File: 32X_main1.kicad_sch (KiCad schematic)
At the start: 26 parts, among them IC504 315-5818, IC505 315-5805, IC509 74AC04

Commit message: General tidying.
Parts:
- removed C912: 10uF, Capacitor_THT:CP_Radial_D5.0mm_P2.50mm, symbol Device:C_Polarized
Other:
- moved on the sheet: C912
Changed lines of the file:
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@@
   (junction (at 96.52 65.405) (diameter 0) (color 0 0 0 0)
   )
-  (junction (at 231.14 250.19) (diameter 0) (color 0 0 0 0)
-  )
   (junction (at 266.7 169.545) (diameter 0) (color 0 0 0 0)
   )
@@
   )
   (junction (at 96.52 79.375) (diameter 0) (color 0 0 0 0)
-  )
-  (junction (at 231.14 238.125) (diameter 0) (color 0 0 0 0)
   )
   (junction (at 96.52 106.68) (diameter 0) (color 0 0 0 0)
@@
     (stroke (width 0) (type default))
   )
-  (wire (pts (xy 231.14 250.19) (xy 243.205 250.19))
-    (stroke (width 0) (type default))
-  )
   (bus (pts (xy 222.885 151.765) (xy 222.885 154.305))
     (stroke (width 0) (type default))
@@
     (stroke (width 0) (type default))
   )
-  (wire (pts (xy 231.14 238.125) (xy 231.14 240.03))
-    (stroke (width 0) (type default))
-  )
   (bus (pts (xy 203.2 83.185) (xy 203.2 80.645))
     (stroke (width 0) (type default))
@@
     (stroke (width 0) (type default))
   )
-  (wire (pts (xy 220.345 250.19) (xy 231.14 250.19))
+  (wire (pts (xy 220.345 250.19) (xy 232.41 250.19))
     (stroke (width 0) (type default))
   )
@@
     (stroke (width 0) (type default))
   )
-  (wire (pts (xy 243.205 238.125) (xy 243.205 240.03))
+  (wire (pts (xy 232.41 238.125) (xy 232.41 240.03))
     (stroke (width 0) (type default))
   )
@@
     (stroke (width 0) (type default))
   )
-  (wire (pts (xy 231.14 250.19) (xy 231.14 247.65))
-    (stroke (width 0) (type default))
-  )
   (wire (pts (xy 90.805 84.455) (xy 96.52 84.455))
     (stroke (width 0) (type default))
@@
     (stroke (width 0) (type default))
   )
-  (wire (pts (xy 243.205 250.19) (xy 243.205 247.65))
+  (wire (pts (xy 232.41 250.19) (xy 232.41 247.65))
     (stroke (width 0) (type default))
   )
@@
     (stroke (width 0) (type default))
   )
-  (wire (pts (xy 220.345 238.125) (xy 231.14 238.125))
-    (stroke (width 0) (type default))
-  )
   (bus (pts (xy 222.885 146.685) (xy 222.885 149.225))
     (stroke (width 0) (type default))
@@
     (stroke (width 0) (type default))
   )
-  (wire (pts (xy 231.14 238.125) (xy 243.205 238.125))
+  (wire (pts (xy 220.345 238.125) (xy 232.41 238.125))
     (stroke (width 0) (type default))
   )
@@
     )
   )
-  (symbol (lib_id "Device:C_Polarized") (at 231.14 243.84 0) (unit 1)
-    (in_bom yes) (on_board yes) (dnp no)
-    (property "Reference" "C912" (at 234.315 245.11 0)
-      (effects (font (size 1.27 1.27)) (justify left))
-    )
-    (property "Value" "10uF" (at 234.315 242.57 0)
-      (effects (font (size 1.27 1.27)) (justify left))
-    )
-    (property "Footprint" "Capacitor_THT:CP_Radial_D5.0mm_P2.50mm" (at 232.1052 247.65 0)
-      (effects (font (size 1.27 1.27)) hide)
-    )
-    (property "Datasheet" "~" (at 231.14 243.84 0)
-      (effects (font (size 1.27 1.27)) hide)
-    )
-    (property "DigiKey" "" (at 231.14 243.84 0)
-      (effects (font (size 1.27 1.27)) hide)
-    )
-    (pin "1")
-    (pin "2")
-    (instances
-      (project "Neptune"
-        (path "/bcc23b51-b742-4ae5-9dd6-d96a24058944/01513199-62c5-4123-a151-ccd381a5e6c1"
-          (reference "C912") (unit 1)
-        )
-        (path "/bcc23b51-b742-4ae5-9dd6-d96a24058944/293c8f1f-2c58-4557-aeb8-8502bb66fbd4"
-          (reference "CE21") (unit 1)
-        )
-        (path "/bcc23b51-b742-4ae5-9dd6-d96a24058944/48e60f61-77cc-4ea0-898f-0029aa970ca5"
-          (reference "CE20") (unit 1)
-        )
-        (path "/bcc23b51-b742-4ae5-9dd6-d96a24058944/0d895458-d3d0-4635-bde5-e15500822f5f"
-          (reference "C30") (unit 1)
-        )
-        (path "/bcc23b51-b742-4ae5-9dd6-d96a24058944/a9caee2e-423b-443e-a11f-5841882e2685"
-          (reference "CE501") (unit 1)
-        )
-      )
-    )
-  )
   (symbol (lib_id "Device:C") (at 195.58 243.84 0) (unit 1)
     (in_bom yes) (on_board yes) (dnp no)
@@
     )
   )
-  (symbol (lib_id "Device:C_Polarized") (at 243.205 243.84 0) (unit 1)
+  (symbol (lib_id "Device:C_Polarized") (at 232.41 243.84 0) (unit 1)
     (in_bom yes) (on_board yes) (dnp no)
-    (property "Reference" "C912" (at 246.38 245.11 0)
+    (property "Reference" "C912" (at 235.585 245.11 0)
       (effects (font (size 1.27 1.27)) (justify left))
     )
-    (property "Value" "10uF" (at 246.38 242.57 0)
+    (property "Value" "10uF" (at 235.585 242.57 0)
       (effects (font (size 1.27 1.27)) (justify left))
     )
-    (property "Footprint" "Capacitor_THT:CP_Radial_D5.0mm_P2.50mm" (at 244.1702 247.65 0)
-      (effects (font (size 1.27 1.27)) hide)
-    )
-    (property "Datasheet" "~" (at 243.205 243.84 0)
-      (effects (font (size 1.27 1.27)) hide)
-    )
-    (property "DigiKey" "" (at 243.205 243.84 0)
-      (effects (font (size 1.27 1.27)) hide)
-    )
+    (property "Footprint" "Capacitor_THT:CP_Radial_D5.0mm_P2.50mm" (at 233.3752 247.65 0)
+      (effects (font (size 1.27 1.27)) hide)
+    )
+    (property "Datasheet" "~" (at 232.41 243.84 0)
+      (effects (font (size 1.27 1.27)) hide)
+    )
+    (property "DigiKey" "" (at 232.41 243.84 0)
+      (effects (font (size 1.27 1.27)) hide)
+    )

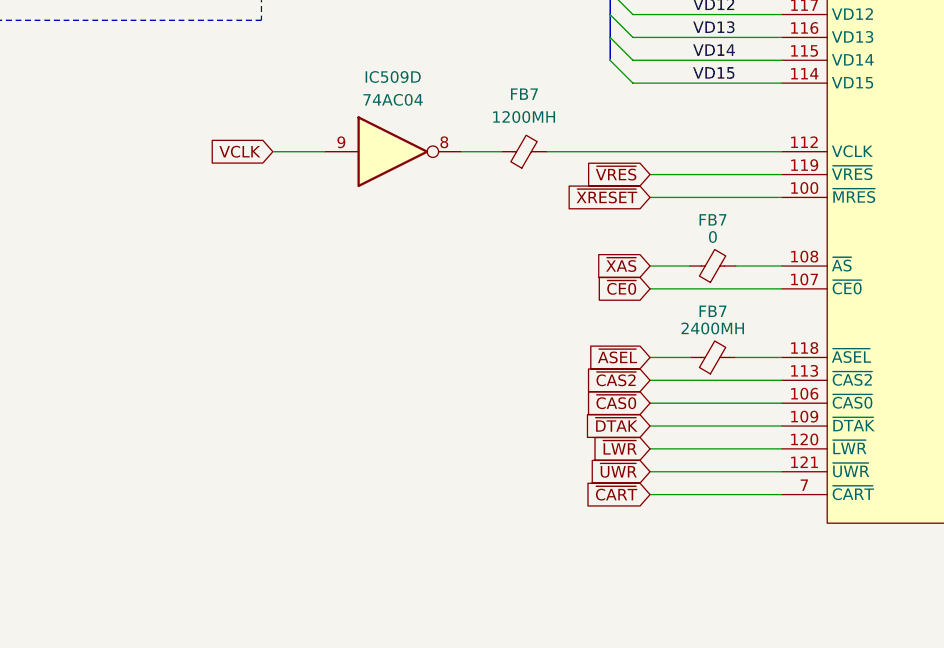
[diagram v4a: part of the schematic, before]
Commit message: Footprint improvements, general tidying.
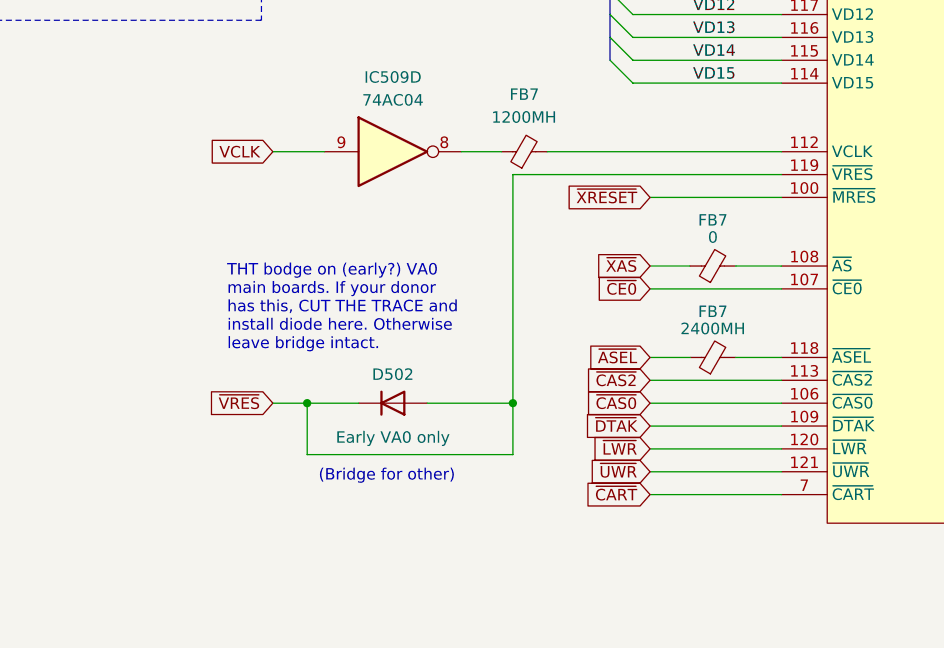
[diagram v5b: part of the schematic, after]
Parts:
- added D502: Early VA0 only, Diode_SMD:D_1206_3216Metric, symbol Device:D
- IC504: footprint Package_QFP:LQFP-176_24x24mm_P0.5mm -> Neptune:LQFP-176_24x24mm_P0.5mm
- L501: footprint Inductor_SMD:L_1206_3216Metric -> Inductor_SMD:L_1210_3225Metric_Pad1.42x2.65mm_HandSolder
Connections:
- net ~{VRES}: now also D502.1 (K), D502.2 (A)
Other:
- note added: "(Bridge for other)"
- note added: "THT bodge on (early?) VA0 main boards. If your donor has this, CUT THE TRACE and install diode here. Otherwise leave bridge intact."
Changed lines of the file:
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@@
   (junction (at 266.7 169.545) (diameter 0) (color 0 0 0 0)
   )
+  (junction (at 131.445 184.785) (diameter 0) (color 0 0 0 0)
+  )
   (junction (at 96.52 67.945) (diameter 0) (color 0 0 0 0)
   )
@@
   (junction (at 96.52 120.65) (diameter 0) (color 0 0 0 0)
   )
+  (junction (at 108.585 184.785) (diameter 0) (color 0 0 0 0)
+  )
   (junction (at 203.835 177.165) (diameter 0) (color 0 0 0 0)
   )
@@
     (stroke (width 0) (type default))
   )
+  (wire (pts (xy 104.775 184.785) (xy 108.585 184.785))
+    (stroke (width 0) (type default))
+  )
   (bus (pts (xy 203.2 67.945) (xy 203.2 65.405))
     (stroke (width 0) (type default))
@@
     (stroke (width 0) (type default))
   )
-  (wire (pts (xy 146.685 159.385) (xy 161.29 159.385))
-    (stroke (width 0) (type default))
-  )
   (wire (pts (xy 191.77 80.645) (xy 200.66 80.645))
     (stroke (width 0) (type default))
@@
     (stroke (width 0) (type default))
   )
+  (wire (pts (xy 121.92 184.785) (xy 131.445 184.785))
+    (stroke (width 0) (type default))
+  )
+  (wire (pts (xy 108.585 184.785) (xy 114.3 184.785))
+    (stroke (width 0) (type default))
+  )
   (bus (pts (xy 203.2 78.105) (xy 203.2 75.565))
     (stroke (width 0) (type default))
@@
     (stroke (width 0) (type default))
   )
+  (wire (pts (xy 131.445 159.385) (xy 131.445 184.785))
+    (stroke (width 0) (type default))
+  )
   (wire (pts (xy 194.945 177.165) (xy 203.835 177.165))
     (stroke (width 0) (type default))
@@
     (stroke (width 0) (type default))
   )
+  (wire (pts (xy 108.585 190.5) (xy 108.585 184.785))
+    (stroke (width 0) (type default))
+  )
   (wire (pts (xy 264.795 50.165) (xy 273.685 50.165))
     (stroke (width 0) (type default))
@@
     (stroke (width 0) (type default))
   )
+  (wire (pts (xy 131.445 159.385) (xy 161.29 159.385))
+    (stroke (width 0) (type default))
+  )
   (wire (pts (xy 234.315 159.385) (xy 225.425 159.385))
     (stroke (width 0) (type default))
@@
     (stroke (width 0) (type default))
   )
+  (wire (pts (xy 131.445 184.785) (xy 131.445 190.5))
+    (stroke (width 0) (type default))
+  )
   (wire (pts (xy 194.945 151.765) (xy 194.945 154.305))
     (stroke (width 0) (type default))
@@
     (stroke (width 0) (type default))
   )
+  (wire (pts (xy 131.445 190.5) (xy 108.585 190.5))
+    (stroke (width 0) (type default))
+  )
   (bus (pts (xy 203.2 47.625) (xy 203.2 50.165))
     (stroke (width 0) (type default))
@@
     (fill (type none))
   )
+  (text "(Bridge for other)" (at 109.855 193.675 0)
+    (effects (font (size 1.27 1.27)) (justify left bottom))
+  )
   (text "VA1 ONLY" (at 91.44 49.53 0)
     (effects (font (size 1.27 1.27)) (justify left bottom))
   )
+  (text "THT bodge on (early?) VA0\nmain boards. If your donor\nhas this, CUT THE TRACE and\ninstall diode here. Otherwise\nleave bridge intact."
+    (at 99.695 179.07 0)
+    (effects (font (size 1.27 1.27)) (justify left bottom))
+  )
   (label "CTD6" (at 194.31 65.405 0) (fields_autoplaced)
     (effects (font (size 1.27 1.27)) (justify left bottom))
@@
     )
   )
-  (global_label "~{VRES}" (shape input) (at 146.685 159.385 180) (fields_autoplaced)
+  (global_label "~{VRES}" (shape input) (at 104.775 184.785 180) (fields_autoplaced)
     (effects (font (size 1.27 1.27)) (justify right))
-    (property "Intersheetrefs" "${INTERSHEET_REFS}" (at 138.9827 159.385 0)
+    (property "Intersheetrefs" "${INTERSHEET_REFS}" (at 97.0727 184.785 0)
       (effects (font (size 1.27 1.27)) (justify right) hide)
     )
@@
     )
   )
+  (symbol (lib_id "Device:D") (at 118.11 184.785 0) (mirror x) (unit 1)
+    (in_bom yes) (on_board yes) (dnp no)
+    (property "Reference" "D502" (at 118.11 181.61 0)
+      (effects (font (size 1.27 1.27)))
+    )
+    (property "Value" "Early VA0 only" (at 118.11 188.595 0)
+      (effects (font (size 1.27 1.27)))
+    )
+    (property "Footprint" "Diode_SMD:D_1206_3216Metric" (at 118.11 184.785 0)
+      (effects (font (size 1.27 1.27)) hide)
+    )
+    (property "Datasheet" "~" (at 118.11 184.785 0)
+      (effects (font (size 1.27 1.27)) hide)
+    )
+    (property "Sim.Device" "D" (at 118.11 184.785 0)
+      (effects (font (size 1.27 1.27)) hide)
+    )
+    (property "Sim.Pins" "1=K 2=A" (at 118.11 184.785 0)
+      (effects (font (size 1.27 1.27)) hide)
+    )
+    (property "DigiKey" "" (at 118.11 184.785 0)
+      (effects (font (size 1.27 1.27)) hide)
+    )
+    (pin "1")
+    (pin "2")
+    (instances
+      (project "Neptune"
+        (path "/bcc23b51-b742-4ae5-9dd6-d96a24058944/edde10e2-ce08-4180-9fbe-ab298dfbfa4c"
+          (reference "D502") (unit 1)
+        )
+        (path "/bcc23b51-b742-4ae5-9dd6-d96a24058944/01513199-62c5-4123-a151-ccd381a5e6c1"
+          (reference "D599") (unit 1)
+        )
+        (path "/bcc23b51-b742-4ae5-9dd6-d96a24058944/a9caee2e-423b-443e-a11f-5841882e2685"
+          (reference "D699") (unit 1)
+        )
+      )
+    )
+  )
   (symbol (lib_id "Device:C_Polarized") (at 232.41 243.84 0) (unit 1)
     (in_bom yes) (on_board yes) (dnp no)
@@
       (effects (font (size 1.27 1.27)) (justify left))
     )
-    (property "Footprint" "Inductor_SMD:L_1206_3216Metric" (at 203.835 170.815 0)
+    (property "Footprint" "Inductor_SMD:L_1210_3225Metric_Pad1.42x2.65mm_HandSolder" (at 203.835 170.815 0)
       (effects (font (size 1.27 1.27)) hide)
     )
@@
       (effects (font (size 1.27 1.27)))
     )
-    (property "Footprint" "Package_QFP:LQFP-176_24x24mm_P0.5mm" (at 176.53 48.26 0)
+    (property "Footprint" "Neptune:LQFP-176_24x24mm_P0.5mm" (at 176.53 48.26 0)
       (effects (font (size 1.27 1.27)) hide)
     )

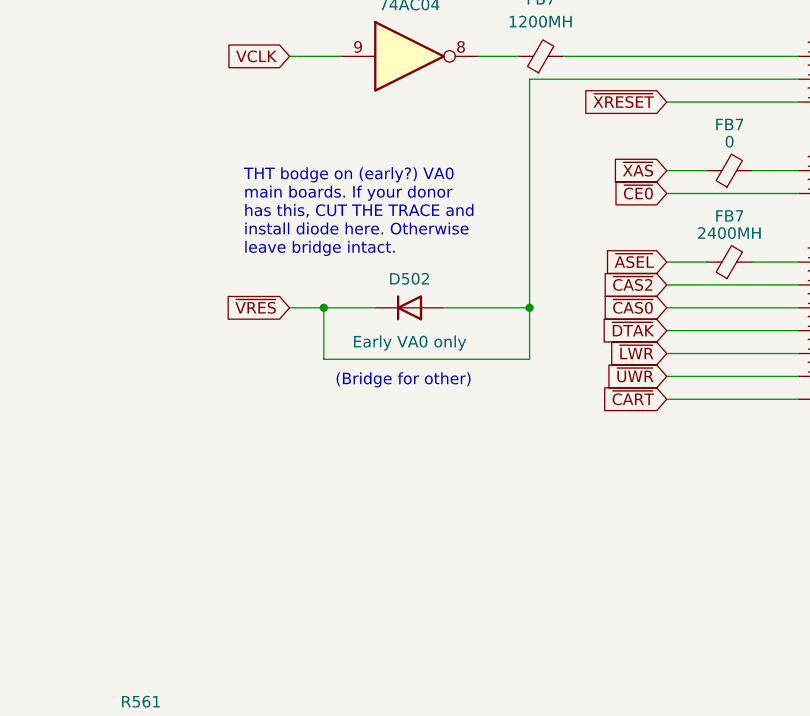
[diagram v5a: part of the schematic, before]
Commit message: Fix note about D699, add footprint for associated capacitor.
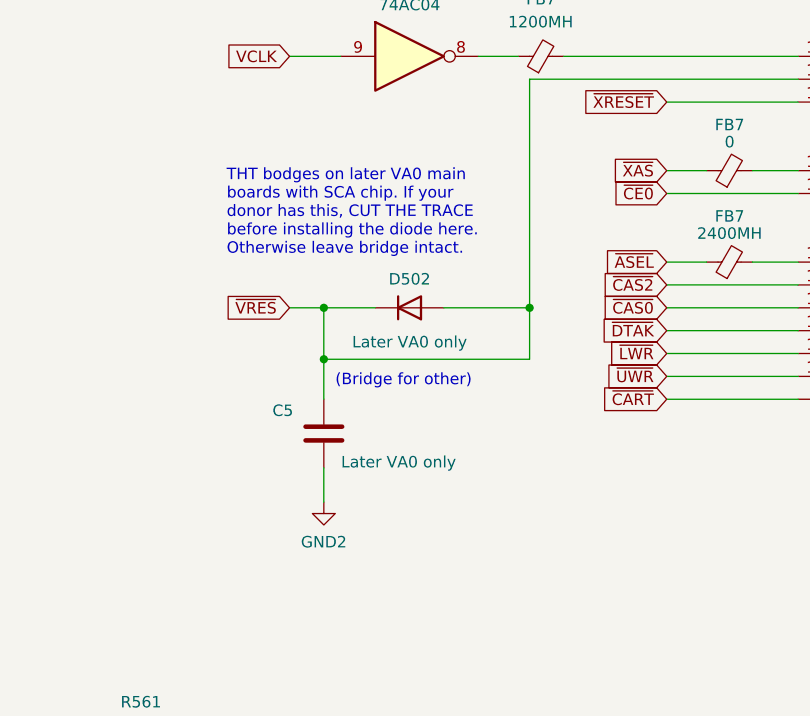
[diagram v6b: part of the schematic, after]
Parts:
- added C5: Later VA0 only, Capacitor_SMD:C_0805_2012Metric, symbol Device:C
- D502: value Early VA0 only -> Later VA0 only
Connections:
- net GND2: now also C5.2
- net ~{VRES}: now also C5.1
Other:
- note added: "THT bodges on later VA0 main boards with SCA chip. If your donor has this, CUT THE TRACE before installing the diode here. Otherwise leave bridge intact."
- note removed: "THT bodge on (early?) VA0 main boards. If your donor has this, CUT THE TRACE and install diode here. Otherwise leave bridge intact."
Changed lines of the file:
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@@
   (junction (at 282.575 151.765) (diameter 0) (color 0 0 0 0)
   )
+  (junction (at 108.585 190.5) (diameter 0) (color 0 0 0 0)
+  )
   (junction (at 266.7 172.085) (diameter 0) (color 0 0 0 0)
   )
@@
     (stroke (width 0) (type default))
   )
+  (wire (pts (xy 108.585 202.565) (xy 108.585 206.375))
+    (stroke (width 0) (type default))
+  )
   (wire (pts (xy 234.315 90.805) (xy 225.425 90.805))
     (stroke (width 0) (type default))
@@
     (stroke (width 0) (type default))
   )
+  (wire (pts (xy 108.585 190.5) (xy 108.585 194.945))
+    (stroke (width 0) (type default))
+  )
   (wire (pts (xy 207.645 238.125) (xy 220.345 238.125))
     (stroke (width 0) (type default))
@@
     (effects (font (size 1.27 1.27)) (justify left bottom))
   )
-  (text "THT bodge on (early?) VA0\nmain boards. If your donor\nhas this, CUT THE TRACE and\ninstall diode here. Otherwise\nleave bridge intact."
-    (at 99.695 179.07 0)
+  (text "THT bodges on later VA0 main\nboards with SCA chip. If your\ndonor has this, CUT THE TRACE\nbefore installing the diode here.\nOtherwise leave bridge intact."
+    (at 97.79 179.07 0)
     (effects (font (size 1.27 1.27)) (justify left bottom))
   )
@@
     )
   )
+  (symbol (lib_id "Device:C") (at 108.585 198.755 0) (unit 1)
+    (in_bom yes) (on_board yes) (dnp no)
+    (property "Reference" "C5" (at 102.87 196.215 0)
+      (effects (font (size 1.27 1.27)) (justify left))
+    )
+    (property "Value" "Later VA0 only" (at 110.49 201.93 0)
+      (effects (font (size 1.27 1.27)) (justify left))
+    )
+    (property "Footprint" "Capacitor_SMD:C_0805_2012Metric" (at 109.5502 202.565 0)
+      (effects (font (size 1.27 1.27)) hide)
+    )
+    (property "Datasheet" "~" (at 108.585 198.755 0)
+      (effects (font (size 1.27 1.27)) hide)
+    )
+    (property "DigiKey" "" (at 108.585 198.755 0)
+      (effects (font (size 1.27 1.27)) hide)
+    )
+    (pin "1")
+    (pin "2")
+    (instances
+      (project "Neptune"
+        (path "/bcc23b51-b742-4ae5-9dd6-d96a24058944/48e60f61-77cc-4ea0-898f-0029aa970ca5"
+          (reference "C5") (unit 1)
+        )
+        (path "/bcc23b51-b742-4ae5-9dd6-d96a24058944/a9caee2e-423b-443e-a11f-5841882e2685"
+          (reference "C695") (unit 1)
+        )
+      )
+    )
+  )
   (symbol (lib_id "power:GND2") (at 96.52 132.715 0) (unit 1)
     (in_bom yes) (on_board yes) (dnp no) (fields_autoplaced)
@@
       (effects (font (size 1.27 1.27)))
     )
-    (property "Value" "Early VA0 only" (at 118.11 188.595 0)
+    (property "Value" "Later VA0 only" (at 118.11 188.595 0)
       (effects (font (size 1.27 1.27)))
     )
@@
         )
       )
+    )
+  )
+  (symbol (lib_id "power:GND2") (at 108.585 206.375 0) (unit 1)
+    (in_bom yes) (on_board yes) (dnp no) (fields_autoplaced)
+    (property "Reference" "#PWR028" (at 108.585 212.725 0)
+      (effects (font (size 1.27 1.27)) hide)
+    )
+    (property "Value" "GND2" (at 108.585 210.82 0)
+      (effects (font (size 1.27 1.27)))
+    )
+    (property "Footprint" "" (at 108.585 206.375 0)
+      (effects (font (size 1.27 1.27)) hide)
+    )
+    (property "Datasheet" "" (at 108.585 206.375 0)
+      (effects (font (size 1.27 1.27)) hide)
+    )
+    (pin "1")
+    (instances
+      (project "Neptune"
+        (path "/bcc23b51-b742-4ae5-9dd6-d96a24058944/01513199-62c5-4123-a151-ccd381a5e6c1"
+          (reference "#PWR028") (unit 1)
+        )
+        (path "/bcc23b51-b742-4ae5-9dd6-d96a24058944/a9caee2e-423b-443e-a11f-5841882e2685"
+          (reference "#PWR091") (unit 1)
+        )
+      )
